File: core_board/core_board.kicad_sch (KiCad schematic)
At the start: 0 parts

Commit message: Add Hierarchical Sheet for Power
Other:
- added sheet Untitled Sheet (Power_in.kicad_sch)
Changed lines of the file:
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@@
 	(generator_version "10.0")
 	(paper "A4")
+	(sheet
+		(at 43.18 53.34)
+		(size 63.5 33.02)
+		(exclude_from_sim no)
+		(in_bom yes)
+		(on_board yes)
+		(dnp no)
+		(fields_autoplaced yes)
+		(stroke
+			(width 0.1524)
+			(type solid)
+		)
+		(fill
+			(color 0 0 0 0)
+		)
+		(property "Sheetname" "Untitled Sheet"
+			(at 43.18 52.6284 0)
+			(show_name no)
+			(do_not_autoplace no)
+			(effects
+				(font
+					(size 1.27 1.27)
+				)
+				(justify left bottom)
+			)
+		)
+		(property "Sheetfile" "Power_in.kicad_sch"
+			(at 43.18 86.9446 0)
+			(show_name no)
+			(do_not_autoplace no)
+			(effects
+				(font
+					(size 1.27 1.27)
+				)
+				(justify left top)
+			)
+		)
+		(instances
+			(project "core_board"
+				(path "/e01d6047-065c-44c8-9643-8ab57e6ffae6"
+					(page "2")
+				)
+			)
+		)
+	)
 	(sheet_instances
 		(path "/"

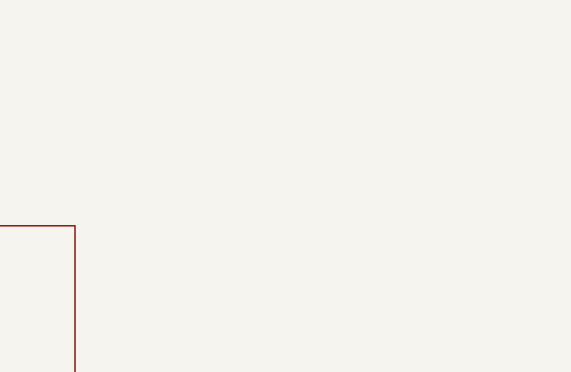
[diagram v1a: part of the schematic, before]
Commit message: Add Temperature sensor Schematic
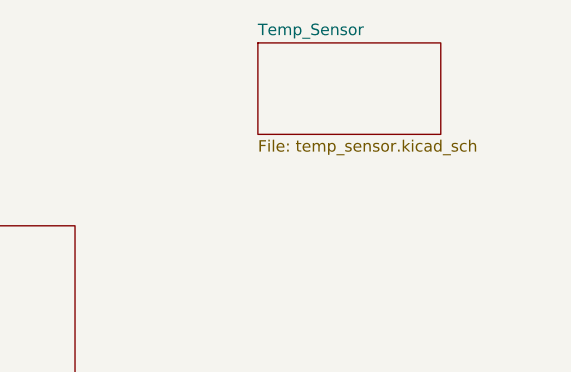
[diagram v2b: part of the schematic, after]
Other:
- added sheet Temp_Sensor (temp_sensor.kicad_sch)
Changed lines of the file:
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@@
 	(paper "A4")
+	(sheet
+		(at 127 33.02)
+		(size 20.32 10.16)
+		(exclude_from_sim no)
+		(in_bom yes)
+		(on_board yes)
+		(dnp no)
+		(fields_autoplaced yes)
+		(stroke
+			(width 0.1524)
+			(type solid)
+		)
+		(fill
+			(color 0 0 0 0)
+		)
+		(property "Sheetname" "Temp_Sensor"
+			(at 127 32.3084 0)
+			(show_name no)
+			(do_not_autoplace no)
+			(effects
+				(font
+					(size 1.27 1.27)
+				)
+				(justify left bottom)
+			)
+		)
+		(property "Sheetfile" "temp_sensor.kicad_sch"
+			(at 127 43.7646 0)
+			(show_name no)
+			(do_not_autoplace no)
+			(effects
+				(font
+					(size 1.27 1.27)
+				)
+				(justify left top)
+			)
+		)
+		(instances
+			(project "core_board"
+				(path "/e01d6047-065c-44c8-9643-8ab57e6ffae6"
+					(page "3")
+				)
+			)
+		)
+	)
 	(sheet
 		(at 43.18 53.34)

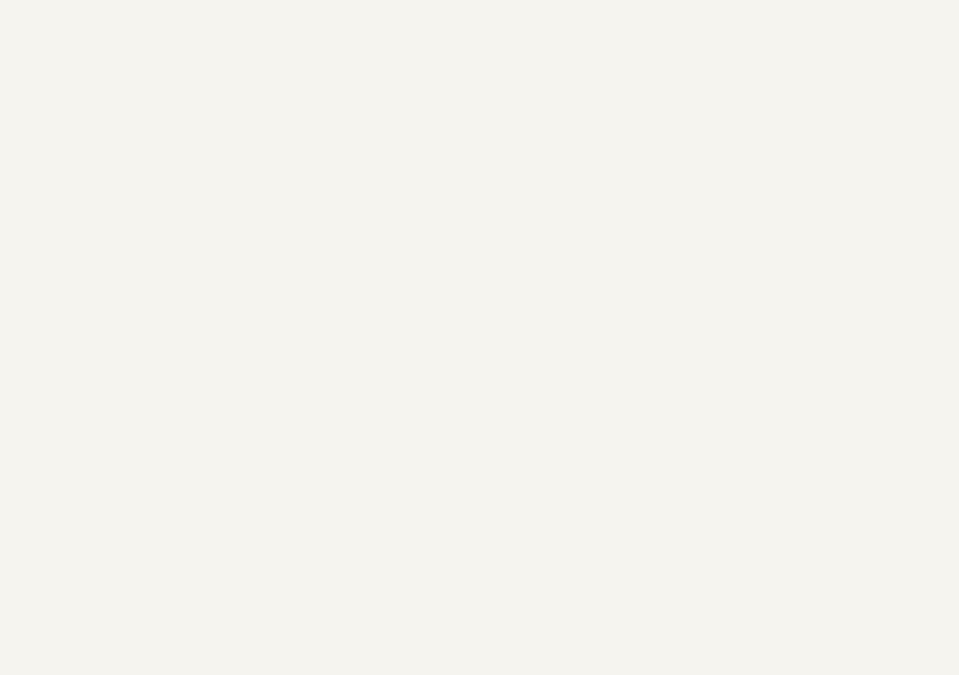
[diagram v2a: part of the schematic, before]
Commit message: add buttons schematic
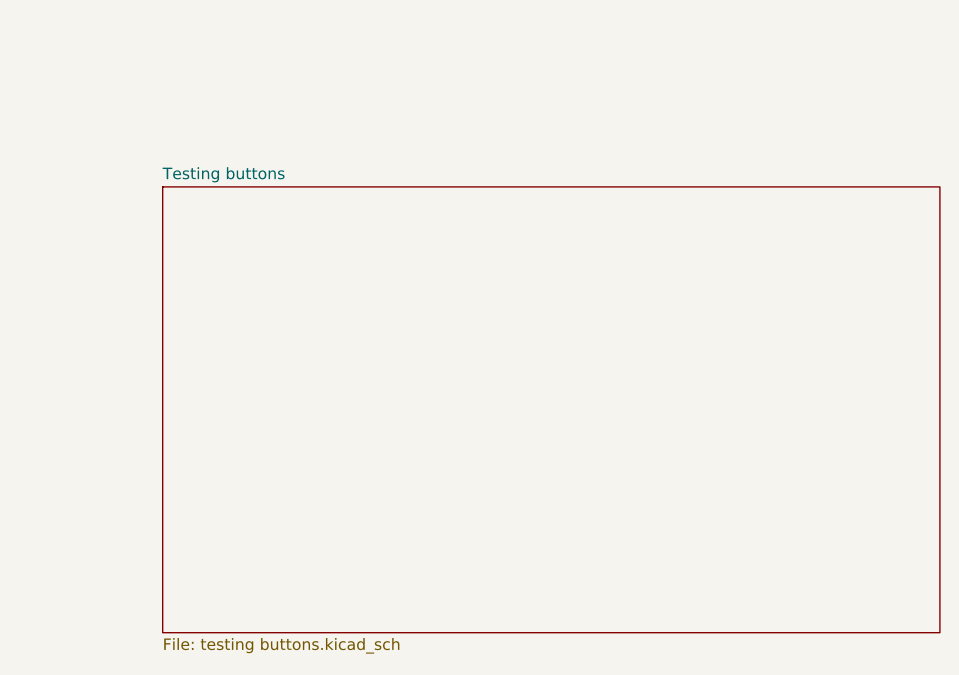
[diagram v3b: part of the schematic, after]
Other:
- added sheet Testing buttons (testing buttons.kicad_sch)
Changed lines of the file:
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@@
 	(paper "A4")
+	(sheet
+		(at 165.1 85.09)
+		(size 86.36 49.53)
+		(exclude_from_sim no)
+		(in_bom yes)
+		(on_board yes)
+		(dnp no)
+		(fields_autoplaced yes)
+		(stroke
+			(width 0.1524)
+			(type solid)
+		)
+		(fill
+			(color 0 0 0 0)
+		)
+		(property "Sheetname" "Testing buttons"
+			(at 165.1 84.3784 0)
+			(show_name no)
+			(do_not_autoplace no)
+			(effects
+				(font
+					(size 1.27 1.27)
+				)
+				(justify left bottom)
+			)
+		)
+		(property "Sheetfile" "testing buttons.kicad_sch"
+			(at 165.1 135.2046 0)
+			(show_name no)
+			(do_not_autoplace no)
+			(effects
+				(font
+					(size 1.27 1.27)
+				)
+				(justify left top)
+			)
+		)
+		(instances
+			(project "core_board"
+				(path "/e01d6047-065c-44c8-9643-8ab57e6ffae6"
+					(page "4")
+				)
+			)
+		)
+	)
 	(sheet
 		(at 127 33.02)

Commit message: Finish Ethernet, Servo Motors, CAN Connector, and SMOCO
Started fans but still need to finalize what type of fan we are using. Microcontroller started still need finished.
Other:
- sheet Untitled Sheet renamed Power
- added sheet Connectors (Connectors.kicad_sch)
- added sheet Microcontroller (Microcontroller.kicad_sch)
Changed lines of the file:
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@@
 	(paper "A4")
 	(sheet
-		(at 165.1 85.09)
-		(size 86.36 49.53)
+		(at 167.64 29.21)
+		(size 53.34 31.75)
 		(exclude_from_sim no)
 		(in_bom yes)
@@
 		)
 		(property "Sheetname" "Testing buttons"
-			(at 165.1 84.3784 0)
+			(at 167.64 28.4984 0)
 			(show_name no)
 			(do_not_autoplace no)
@@
 		)
 		(property "Sheetfile" "testing buttons.kicad_sch"
-			(at 165.1 135.2046 0)
+			(at 167.64 61.5446 0)
 			(show_name no)
 			(do_not_autoplace no)
@@
 	)
 	(sheet
-		(at 127 33.02)
-		(size 20.32 10.16)
+		(at 167.64 71.12)
+		(size 55.88 27.94)
+		(exclude_from_sim no)
+		(in_bom yes)
+		(on_board yes)
+		(dnp no)
+		(fields_autoplaced yes)
+		(stroke
+			(width 0.1524)
+			(type solid)
+		)
+		(fill
+			(color 0 0 0 0)
+		)
+		(property "Sheetname" "Connectors"
+			(at 167.64 70.4084 0)
+			(show_name no)
+			(do_not_autoplace no)
+			(effects
+				(font
+					(size 1.27 1.27)
+				)
+				(justify left bottom)
+			)
+		)
+		(property "Sheetfile" "Connectors.kicad_sch"
+			(at 167.64 99.6446 0)
+			(show_name no)
+			(do_not_autoplace no)
+			(effects
+				(font
+					(size 1.27 1.27)
+				)
+				(justify left top)
+			)
+		)
+		(instances
+			(project "core_board"
+				(path "/e01d6047-065c-44c8-9643-8ab57e6ffae6"
+					(page "6")
+				)
+			)
+		)
+	)
+	(sheet
+		(at 109.22 21.59)
+		(size 35.56 115.57)
+		(exclude_from_sim no)
+		(in_bom yes)
+		(on_board yes)
+		(dnp no)
+		(fields_autoplaced yes)
+		(stroke
+			(width 0.1524)
+			(type solid)
+		)
+		(fill
+			(color 0 0 0 0)
+		)
+		(property "Sheetname" "Microcontroller"
+			(at 109.22 20.8784 0)
+			(show_name no)
+			(do_not_autoplace no)
+			(effects
+				(font
+					(size 1.27 1.27)
+				)
+				(justify left bottom)
+			)
+		)
+		(property "Sheetfile" "Microcontroller.kicad_sch"
+			(at 109.22 137.7446 0)
+			(show_name no)
+			(do_not_autoplace no)
+			(effects
+				(font
+					(size 1.27 1.27)
+				)
+				(justify left top)
+			)
+		)
+		(instances
+			(project "core_board"
+				(path "/e01d6047-065c-44c8-9643-8ab57e6ffae6"
+					(page "5")
+				)
+			)
+		)
+	)
+	(sheet
+		(at 20.32 59.69)
+		(size 63.5 21.59)
 		(exclude_from_sim no)
 		(in_bom yes)
@@
 		)
 		(property "Sheetname" "Temp_Sensor"
-			(at 127 32.3084 0)
+			(at 20.32 58.9784 0)
 			(show_name no)
 			(do_not_autoplace no)
@@
 		)
 		(property "Sheetfile" "temp_sensor.kicad_sch"
-			(at 127 43.7646 0)
+			(at 20.32 81.8646 0)
 			(show_name no)
 			(do_not_autoplace no)
@@
 	)
 	(sheet
-		(at 43.18 53.34)
+		(at 20.32 19.05)
 		(size 63.5 33.02)
 		(exclude_from_sim no)
@@
 			(color 0 0 0 0)
 		)
-		(property "Sheetname" "Untitled Sheet"
-			(at 43.18 52.6284 0)
+		(property "Sheetname" "Power"
+			(at 20.32 18.3384 0)
 			(show_name no)
 			(do_not_autoplace no)
@@
 		)
 		(property "Sheetfile" "Power_in.kicad_sch"
-			(at 43.18 86.9446 0)
-			(show_name no)
-			(do_not_autoplace no)
+			(at 20.32 52.6546 0)
+			(show_name no)
+			(do_not_autoplace no)

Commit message: Finish Schematic
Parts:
- added H1, H2, H3, H4: MountingHole, symbol Mechanical:MountingHole
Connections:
- no-connect marks 0 -> 3
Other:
- sheet Connectors ports: added BLUE_PWM_Internal, BLUE_PWM_StateDisplay, BackPan, BackTilt, CANHigh, CANLow, FanPWM1, FanPWM2, FanPWM3, GREEN_PWM_Internal, GREEN_PWM_StateDisplay, LeftPan, LeftTilt, RED_PWM_Internal, RED_PWM_StateDisplay, RightPan, RightTilt, Spare1, Spare2, Tach1, Tach2, Tach3; removed none
- sheet Microcontroller ports: added BLUE_PWM_Internal, BLUE_PWM_StateDisplay, BackPan_PWM, BackTilt_PWM, CANHigh, CANLow, Direction_Switch, Down, Fan1PWM, Fan2PWM, Fan3PWM, GREEN_PWM_Internal, GREEN_PWM_StateDisplay, Left, LeftPAN_PWM, LeftTilt_PWM, PanBack_LED, PanLeft_LED, PanRight_LED, RED_PWM_Internal, RED_PWM_StateDisplay, RTRY1, RTRY2, RTRY4, Right, RightPAN_PWM, RightTilt_PWM, SMOCO_LED, Spare1_PWM, Spare2_PWM, TEMP_OUT, TiltBack_LED, TiltLeft_LED, TiltRight_LED, Up; removed none
- sheet Temp_Sensor ports: added TEMP_OUT; removed none
- sheet Testing buttons ports: added Direction_Switch, Down, Left, PanBack_LED, PanLeft_LED, PanRight_LED, RTRY1, RTRY2, RTRY4, Right, SMOCO_LED, TiltBack_LED, TiltLeft_LED, TiltRight_LED, Up; removed none

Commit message: Pull down resisters
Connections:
- no-connect marks 3 -> 0
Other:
- sheet Connectors ports: added none; removed Tach1, Tach2, Tach3
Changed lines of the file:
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@@
 	(generator_version "10.0")
 	(paper "A4")
-	(no_connect
-		(at 149.86 115.57)
-	)
-	(no_connect
-		(at 149.86 118.11)
-	)
-	(no_connect
-		(at 149.86 120.65)
-	)
 	(wire
 		(pts
@@
 			(effects
 				(font
-					(size 1.27 1.27)
-				)
-				(justify left)
-			)
-		)
-		(pin "Tach1" input
-			(at 149.86 115.57 180)
-			(effects
-				(font
-					(size 1.27 1.27)
-				)
-				(justify left)
-			)
-		)
-		(pin "Tach2" input
-			(at 149.86 118.11 180)
-			(effects
-				(font
-					(size 1.27 1.27)
-				)
-				(justify left)
-			)
-		)
-		(pin "Tach3" input
-			(at 149.86 120.65 180)
-			(effects
-				(font

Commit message: add
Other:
- sheet Microcontroller ports: added none; removed Spare1_PWM
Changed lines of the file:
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@@
-			)
-		)
-		(pin "Spare1_PWM" output
-			(at 144.78 99.06 0)
-			(effects
-				(font
-					(size 1.27 1.27)
-				)
-				(justify right)
 			)
 		)

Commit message: add
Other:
- sheet Connectors ports: added electromagnet; removed Spare1
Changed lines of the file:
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@@
+		)
+	)
+	(hierarchical_label "electromagnet"
+		(shape input)
+		(at 144.78 99.06 180)
+		(effects
+			(font
+				(size 1.27 1.27)
+			)
+			(justify right)
 		)
 	)
@@
 			)
 		)
-		(pin "Spare1" input
+		(pin "electromagnet" input
 			(at 149.86 99.06 180)
 			(effects
